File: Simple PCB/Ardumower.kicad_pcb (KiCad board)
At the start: 2 copper layers, 182.1 x 95.7 mm, 56 parts, among them J1 9V IN, J10 Sonar_R, J11 Sonar_C, J12 Sonar_L, J13 P_Right, J14 24V IN, J15 P_Left, J16 DS3231 RTC, J17 Button, J18 ODO_Right, J19 ODO_Left, J2 I2C_1, J20 Remote, J21 PCB_2, J22 3.3V, J23 GND, J24 RX & TX, J3 I2C_2, J4 I2C_3, J5 Bumper, J6 Drop_Left, J7 Drop_Right, J8 Tilt, J9 Rain, U1 MC33926, U2 MC33926

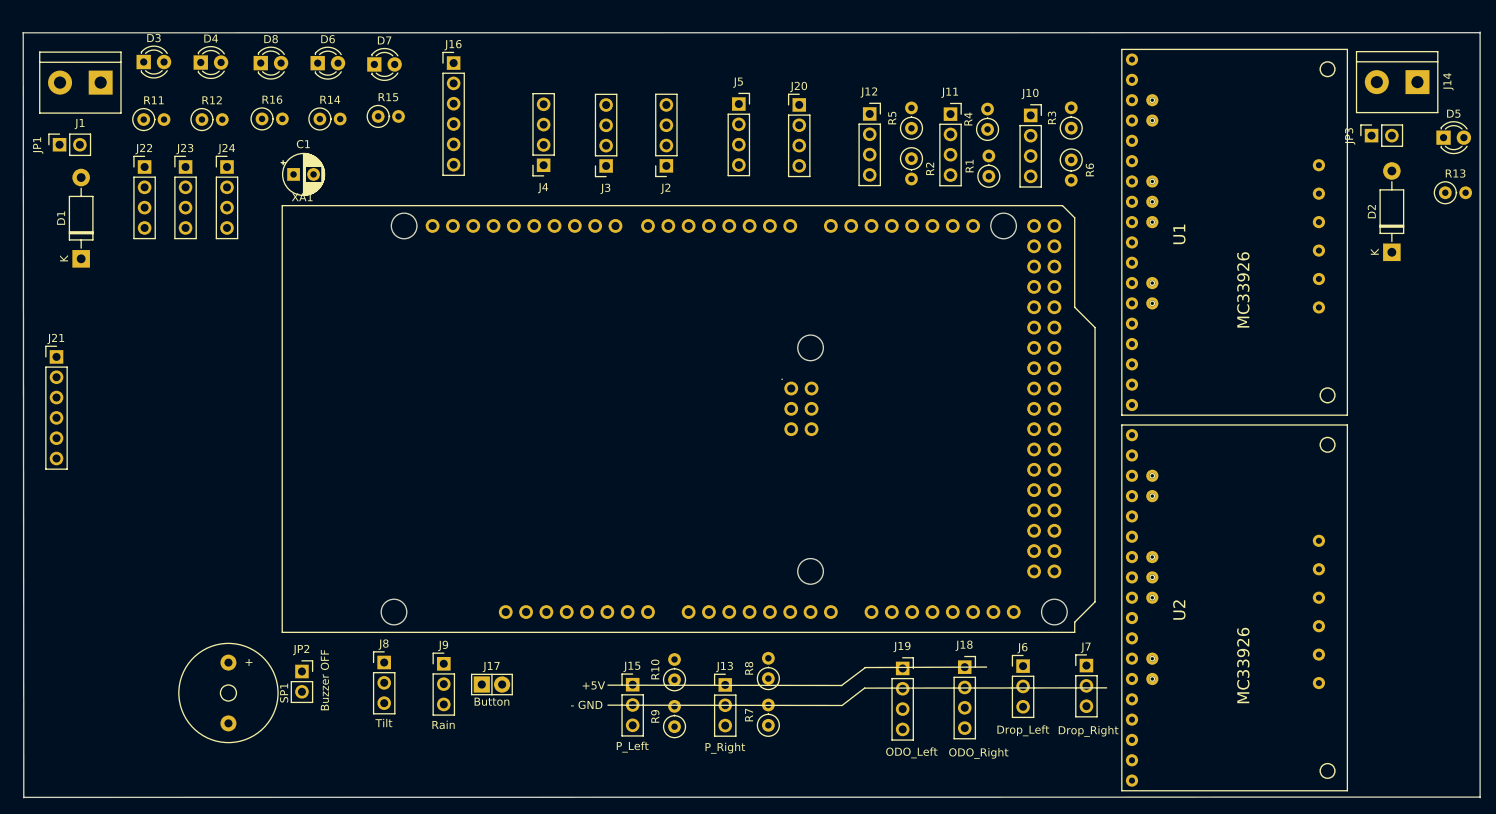
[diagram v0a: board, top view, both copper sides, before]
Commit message: Starsurfer78
Sorting the Footprints on PCB
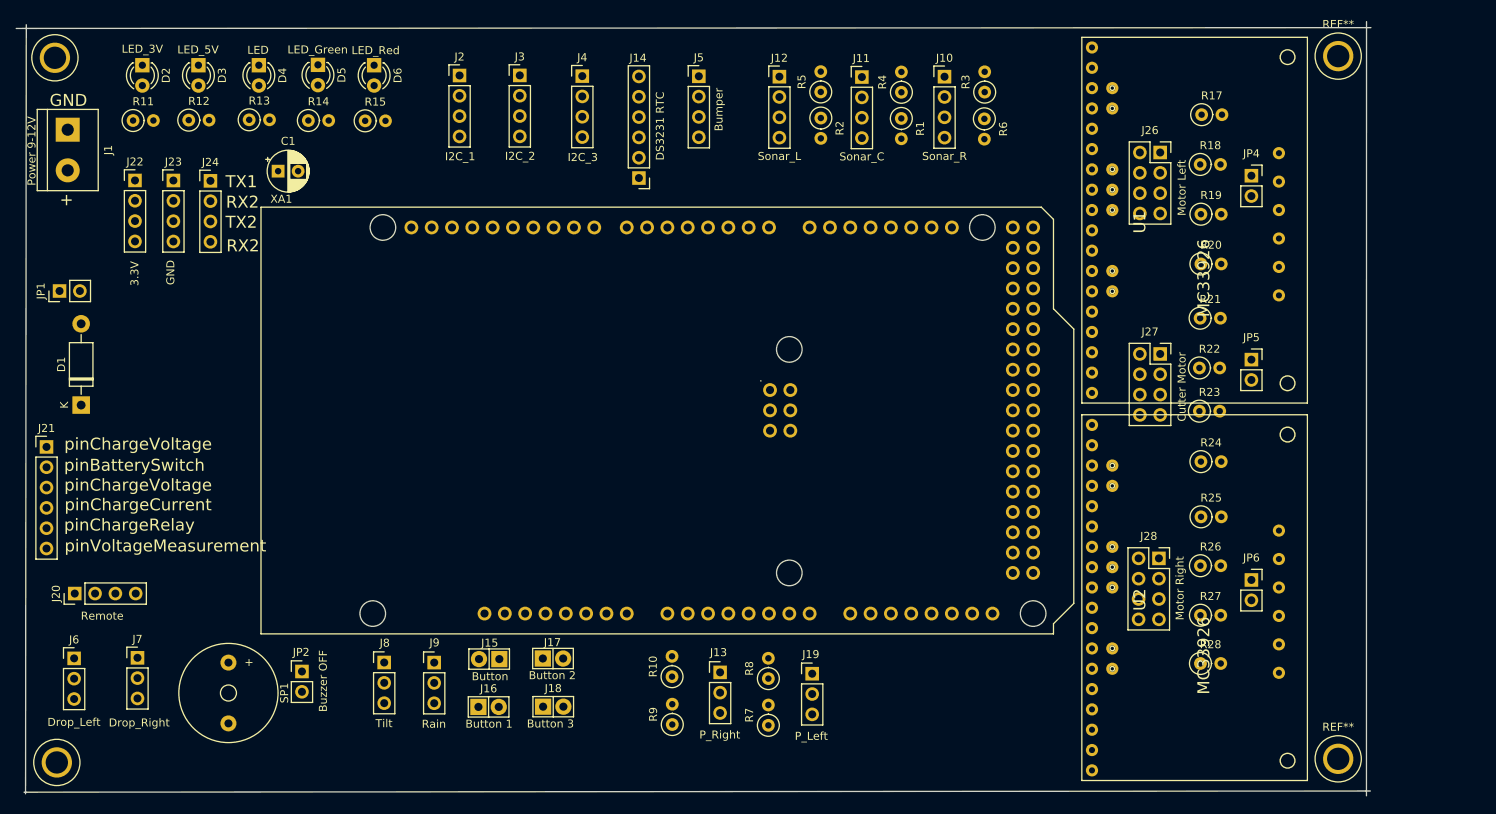
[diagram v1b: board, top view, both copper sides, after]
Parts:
- removed the D5 at (217.9, 49.2)
- removed D8: LED_Red, LED_THT:LED_D3.0mm
- removed the J14 at (214.7, 42.2)
- removed the J22 at (55.6, 52.9)
- removed JP3: 24V, Connector_PinSocket_2.54mm:PinSocket_1x02_P2.54mm_Vertical
- removed the R13 at (218.2, 56.1)
- added J16: Button 1, Zimprich:Pin_Header_KK110_1x02_3D, F.Cu at (98.6, 120.3)
- added J19: P_Left, Connector_PinHeader_2.54mm:PinHeader_1x03_P2.54mm_Vertical, F.Cu at (139.0, 116.2)
- added J26: Motor Left, Connector_PinSocket_2.54mm:PinSocket_2x04_P2.54mm_Vertical, F.Cu at (182.5, 51.0)
- added J27: Cutter Motor, Connector_PinSocket_2.54mm:PinSocket_2x04_P2.54mm_Vertical, F.Cu at (182.5, 76.2)
- added J28: Motor Right, Connector_PinSocket_2.54mm:PinSocket_2x04_P2.54mm_Vertical, F.Cu at (182.3, 101.8)
- added JP4: 5V, Connector_PinSocket_2.54mm:PinSocket_1x02_P2.54mm_Vertical, F.Cu at (193.9, 53.9)
- added JP5: 5V, Connector_PinSocket_2.54mm:PinSocket_1x02_P2.54mm_Vertical, F.Cu at (193.9, 76.9)
- added JP6: 5V, Connector_PinSocket_2.54mm:PinSocket_1x02_P2.54mm_Vertical, F.Cu at (193.9, 104.5)
- added R17: 1.5KO, Resistor_THT:R_Axial_DIN0207_L6.3mm_D2.5mm_P2.54mm_Vertical, F.Cu at (187.7, 46.3)
- added R18: 1KO, Resistor_THT:R_Axial_DIN0207_L6.3mm_D2.5mm_P2.54mm_Vertical, F.Cu at (187.5, 52.5)
- added R19: 1.5KO, Resistor_THT:R_Axial_DIN0207_L6.3mm_D2.5mm_P2.54mm_Vertical, F.Cu at (187.6, 58.8)
- added R20: 1KO, Resistor_THT:R_Axial_DIN0207_L6.3mm_D2.5mm_P2.54mm_Vertical, F.Cu at (187.6, 65.0)
- added R21: 1.5KO, Resistor_THT:R_Axial_DIN0207_L6.3mm_D2.5mm_P2.54mm_Vertical, F.Cu at (187.5, 71.8)
- added R22: 1KO, Resistor_THT:R_Axial_DIN0207_L6.3mm_D2.5mm_P2.54mm_Vertical, F.Cu at (187.4, 78.0)
- added R23: 1.5KO, Resistor_THT:R_Axial_DIN0207_L6.3mm_D2.5mm_P2.54mm_Vertical, F.Cu at (187.4, 83.4)
- added R24: 1KO, Resistor_THT:R_Axial_DIN0207_L6.3mm_D2.5mm_P2.54mm_Vertical, F.Cu at (187.6, 89.7)
- added R25: 1.5KO, Resistor_THT:R_Axial_DIN0207_L6.3mm_D2.5mm_P2.54mm_Vertical, F.Cu at (187.6, 96.6)
- added R26: 1KO, Resistor_THT:R_Axial_DIN0207_L6.3mm_D2.5mm_P2.54mm_Vertical, F.Cu at (187.5, 102.7)
- added R27: 1.5KO, Resistor_THT:R_Axial_DIN0207_L6.3mm_D2.5mm_P2.54mm_Vertical, F.Cu at (187.5, 108.9)
- added R28: 1KO, Resistor_THT:R_Axial_DIN0207_L6.3mm_D2.5mm_P2.54mm_Vertical, F.Cu at (187.5, 114.9)
- added REF**: Test-Point-Pin_Drill2.79mm, digikey-footprints:Test-Point-Pin_Drill2.79mm, F.Cu at (44.4, 39.2)
- added REF**: Test-Point-Pin_Drill2.79mm, digikey-footprints:Test-Point-Pin_Drill2.79mm, F.Cu at (44.6, 127.3)
- added REF**: Test-Point-Pin_Drill2.79mm, digikey-footprints:Test-Point-Pin_Drill2.79mm, F.Cu at (204.8, 126.8)
- added REF**: Test-Point-Pin_Drill2.79mm, digikey-footprints:Test-Point-Pin_Drill2.79mm, F.Cu at (204.8, 39.0)
- D2: value 1N5819 -> LED_3V; footprint Diode_THT:D_DO-41_SOD81_P10.16mm_Horizontal -> LED_THT:LED_D3.0mm
- D3: value LED_3V -> LED_5V
- D4: value LED_5V -> LED
- D5: renamed from D6; value LED -> LED_Green
- D6: renamed from D7; value LED_Green -> LED_Red
- J1: value 9V IN -> Power 9-12V
- J10, J11, J12, J2, J3, J4, J5: footprint Connector_PinSocket_2.54mm:PinSocket_1x04_P2.54mm_Vertical -> Connector_PinHeader_2.54mm:PinHeader_1x04_P2.54mm_Vertical
- J14: renamed from J15; value P_Left -> DS3231 RTC; footprint Connector_PinHeader_2.54mm:PinHeader_1x03_P2.54mm_Vertical -> Connector_PinHeader_2.54mm:PinHeader_1x06_P2.54mm_Vertical
- J15: renamed from J16; value DS3231 RTC -> Button; footprint Connector_PinHeader_2.54mm:PinHeader_1x06_P2.54mm_Vertical -> Zimprich:Pin_Header_KK110_1x02_3D
- J17: value Button -> Button 2
- J18: value ODO_Right -> Button 3; footprint Connector_PinSocket_2.54mm:PinSocket_1x04_P2.54mm_Vertical -> Zimprich:Pin_Header_KK110_1x02_3D
- J20: renamed from J19; value ODO_Left -> Remote; footprint Connector_PinSocket_2.54mm:PinSocket_1x04_P2.54mm_Vertical -> Connector_PinHeader_2.54mm:PinHeader_1x04_P2.54mm_Vertical
- J21: renamed from J20; value Remote -> PCB_2; footprint Connector_PinHeader_2.54mm:PinHeader_1x04_P2.54mm_Vertical -> Connector_PinHeader_2.54mm:PinHeader_1x06_P2.54mm_Vertical
- J22: renamed from J21; value PCB_2 -> 3.3V; footprint Connector_PinHeader_2.54mm:PinHeader_1x06_P2.54mm_Vertical -> Connector_PinHeader_2.54mm:PinHeader_1x04_P2.54mm_Vertical
- JP1, JP2: footprint Connector_PinSocket_2.54mm:PinSocket_1x02_P2.54mm_Vertical -> Connector_PinHeader_2.54mm:PinHeader_1x02_P2.54mm_Vertical
- moved D2 157.9 mm to (55.3, 40.1), turned to 270 degrees
- moved J6 118.6 mm to (46.8, 114.3)
- moved J7 118.6 mm to (54.7, 114.2)
- moved J20 103.9 mm to (46.8, 106.2), turned to 90 degrees
- moved J21 103.3 mm to (43.3, 87.8)
- moved J15 74.6 mm to (98.6, 114.4), turned to 180 degrees
- moved J14 63.3 mm to (117.3, 54.2), turned to 180 degrees
- moved J18 51.7 mm to (106.6, 120.3)
- moved J2 28.2 mm to (94.9, 41.4), turned to 0 degrees
- moved J22 24.1 mm to (54.4, 54.5)
- moved D1 18.3 mm to (47.6, 82.6)
- moved JP1 18.3 mm to (44.9, 68.3)
- moved J3 15.6 mm to (102.5, 41.4), turned to 0 degrees
- moved R1 13.1 mm to (150.2, 46.8), turned to 270 degrees
- moved R15 12.9 mm to (83.1, 47.1)
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- renumbered R14 to R13, R15 to R14, R16 to R15
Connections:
- D2 pad 1: +24V -> GND
- D5 pad 2: Net-(D6-Pad2) -> Net-(D5-Pad2)
- D6 pad 2: Net-(D7-Pad2) -> Net-(D6-Pad2)
- J14 pad 1: +5V -> Net-(J14-Pad1)
- J14 pad 2: GND -> Net-(J14-Pad2)
- J14 pad 3: Net-(J15-Pad3) -> SCL1
- J15 pad 1: Net-(J16-Pad1) -> GND
- J15 pad 2: Net-(J16-Pad2) -> pinButton
- J17 pad 2: pinButton -> pinUserSwitch2
- J18 pad 1: +5V -> GND
- J18 pad 2: GND -> pinUserSwitch3
- J20 pad 1: +5V -> pinRemoteSpeed
- J20 pad 2: GND -> pinRemoteSteer
- J20 pad 3: pinOdometryLeft -> pinRemoteMow
- J20 pad 4: pinOdometryLeft2 -> pinRemoteSwitch
- J21 pad 1: pinRemoteSpeed -> pinBatteryVoltage
- J21 pad 2: pinRemoteSteer -> pinBatterySwitch
- J21 pad 3: pinRemoteMow -> pinChargeVoltage
- J21 pad 4: pinRemoteSwitch -> pinChargeCurrent
- J22 pad 1: pinBatteryVoltage -> +3V3
- J22 pad 2: pinBatterySwitch -> +3V3
- J22 pad 3: pinChargeVoltage -> +3V3
- J22 pad 4: pinChargeCurrent -> +3V3
- R10 pad 1: Net-(J15-Pad3) -> Net-(J19-Pad3)
- R11 pad 1: Net-(D3-Pad2) -> Net-(D2-Pad2)
- R12 pad 1: Net-(D4-Pad2) -> Net-(D3-Pad2)
- R13 pad 2: Net-(D6-Pad2) -> Net-(D4-Pad2)
- R14 pad 2: Net-(D7-Pad2) -> Net-(D5-Pad2)
- R15 pad 2: Net-(D8-Pad2) -> Net-(D6-Pad2)
- R9 pad 1: Net-(J15-Pad3) -> Net-(J19-Pad3)
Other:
- board size 182.1 x 95.7 mm -> 169.3 x 96.8 mm
- board text added: "+"
- board text added: "GND"
- board text added: "RX2"
- board text added: "TX1"
- board text added: "TX2"
- board text added: "pinBatterySwitch"
- board text added: "pinChargeCurrent"
- board text added: "pinChargeRelay"
- board text added: "pinChargeVoltage"
- board text added: "pinVoltageMeasurement"
- board text removed: "+5V"
- board text removed: "- GND"
